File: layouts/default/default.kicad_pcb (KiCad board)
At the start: 2 copper layers, 50 x 50 mm, 37 parts

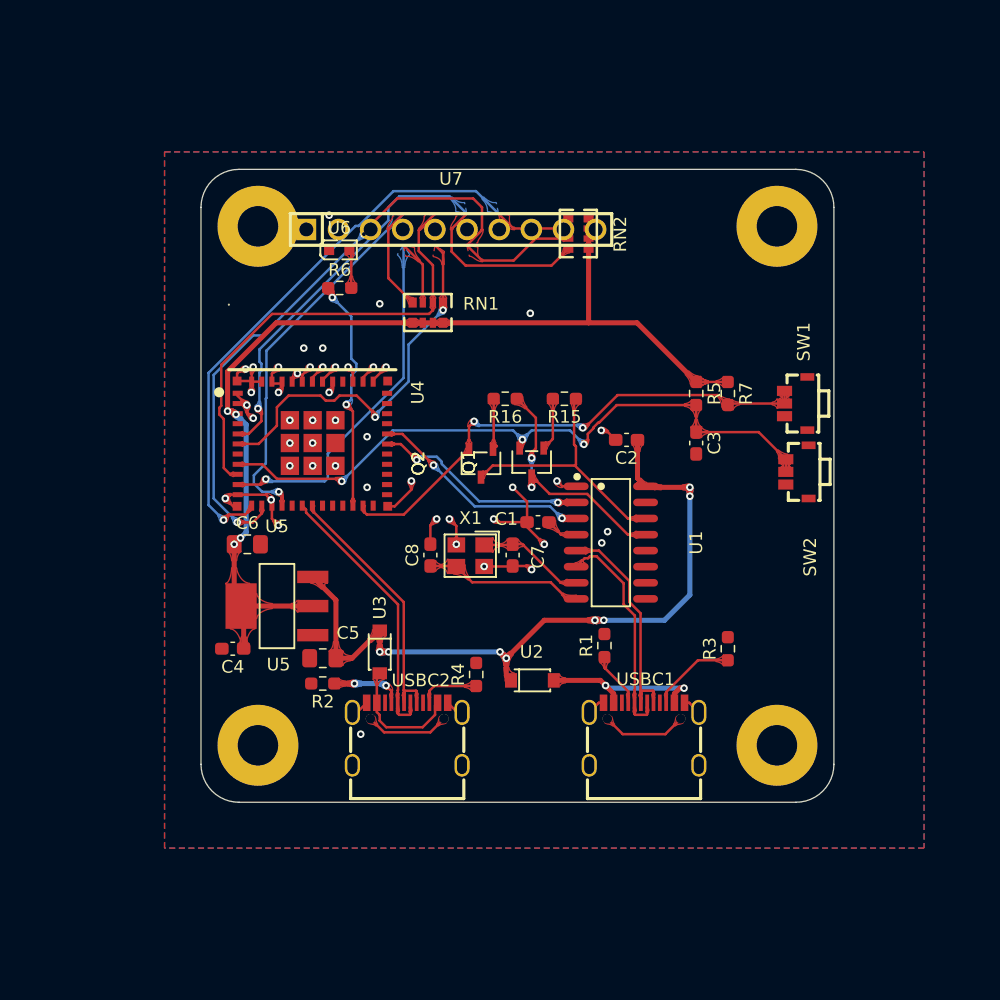
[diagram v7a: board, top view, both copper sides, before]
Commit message: New footprint for C6
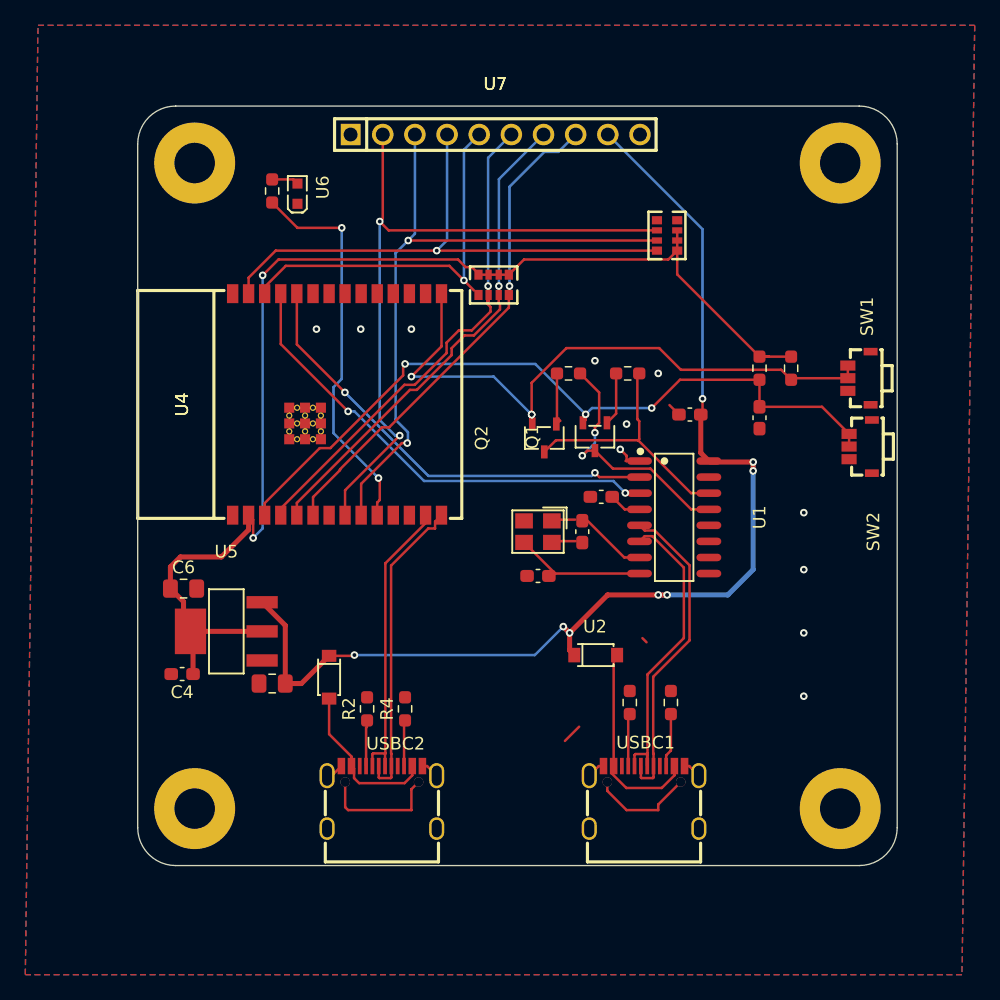
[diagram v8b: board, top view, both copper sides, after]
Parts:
- U4: footprint Espressif_Systems_ESP32_C6_MINI_1_N4:WIFIM-SMD_61P-L16.6-W13.2-P0.80-ESP32-C6-MINI-1-N4 -> Espressif_Systems_ESP32_C6_WROOM_1_N8:WIRELM-SMD_ESP32-C6-WROOM-1
- moved R6 9.34 mm to (98.5, 73.1), turned to 90 degrees
- moved C8 8.66 mm to (119.5, 103.5), turned to 180 degrees
- moved U7 8.28 mm to (116.1, 68.6)
- moved H1 7.07 mm to (92.4, 70.9)
- moved H2 7.07 mm to (143.4, 70.9)
- moved H3 7.07 mm to (92.4, 121.9)
- moved H4 7.07 mm to (143.4, 121.9)
- moved RN2 7.00 mm to (129.7, 76.6)
- moved R4 6.24 mm to (109.0, 114.0)
- moved R3 6.19 mm to (130.0, 113.5)
- moved C6 6.13 mm to (91.5, 104.5)
- moved C7 5.80 mm to (123.0, 100.0)
- moved X1 5.68 mm to (119.5, 100.0)
- moved RN1 5.65 mm to (116.0, 80.5), turned to 180 degrees
- moved U6 5.54 mm to (100.5, 73.3), turned to 90 degrees
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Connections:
- U4 pad 10: IO5 -> IO8
- U4 pad 11: GND -> IO10
- U4 pad 12: IO0 -> IO11
- U4 pad 13: IO1 -> esp32-D_N
- U4 pad 14: GND -> esp32-D_P
- U4 pad 15: IO6 -> boot_pullup-E
- U4 pad 16: IO7 -> IO18
- U4 pad 17: esp32-D_N -> IO19
- U4 pad 18: esp32-D_P -> IO20
- U4 pad 19: IO14 -> IO21
- U4 pad 2: GND -> power_3v3-VCC
- U4 pad 20: IO15 -> IO22
- U4 pad 21: esp32-net-0 -> IO23
- U4 pad 22: IO8 -> esp32-net-1
- U4 pad 23: boot_pullup-E -> IO15
- U4 pad 24: IO18 -> TXD
- U4 pad 25: IO19 -> RXD
- U4 pad 26: IO20 -> IO3
- U4 pad 27: IO21 -> IO2
- U4 pad 28: IO22 -> GND
- U4 pad 29: IO23 -> GND
- U4 pad 3: power_3v3-VCC -> btn_reset-E
- U4 pad 30: TXD -> GND
- U4 pad 31: RXD -> GND
- U4 pad 32: esp32-net-1 -> GND
- U4 pad 33: esp32-net-2 -> GND
- U4 pad 34: esp32-net-3 -> GND
- U4 pad 35: esp32-net-4 -> GND
- U4 pad 4: esp32-net-5 -> IO4
- U4 pad 5: IO2 -> IO5
- U4 pad 6: IO3 -> IO6
- U4 pad 7: esp32-net-6 -> IO7
- U4 pad 8: btn_reset-E -> IO0
- U4 pad 9: IO4 -> IO1
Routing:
- net GND: track 56.4 -> 10.8 mm, vias 47 -> 11
- net power_5v-VCC: track 60.6 -> 93.4 mm
- net RXD: track 17.7 -> 38.3 mm
- net TXD: track 17.2 -> 35.6 mm
- net power_3v3-VCC: track 81.7 -> 95.4 mm, vias 4 -> 2
- net IO8: track 18.2 -> 30.9 mm
- net boot_pullup-E: track 40.5 -> 49.7 mm, vias 2 -> 3
- net ch340g-D_P: track 18.0 -> 25.2 mm
- net ch340g-D_N: track 17.6 -> 24.4 mm
- net btn_reset-E: track 53.1 -> 59.7 mm
- net IO5: track 33.5 -> 39.0 mm
- net IO0: track 50.3 -> 55.0 mm, vias 1 -> 2
- net diode_esp-VBUS: track 9.36 -> 12.8 mm
- net esp32-D_P: track 21.4 -> 24.6 mm
- net footprint-net-1: track 6.69 -> 9.77 mm
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- removed copper zone on F.Cu, net A
- removed copper zone on B.Cu, net IO0
- removed copper zone on F.Cu, net IO0
- removed copper zone on B.Cu, net IO1
- removed copper zone on F.Cu, net IO1
- removed copper zone on B.Cu, net IO2
- removed copper zone on F.Cu, net IO2
- removed copper zone on B.Cu, net IO3
- removed copper zone on F.Cu, net IO3
- removed copper zone on F.Cu, net IO4
- removed copper zone on B.Cu, net IO5
- removed copper zone on F.Cu, net IO5
- removed copper zone on B.Cu, net IO6
- removed copper zone on F.Cu, net IO6
- removed copper zone on B.Cu, net IO8
- removed copper zone on F.Cu, net IO8
- removed copper zone on B.Cu, net RXD
- removed copper zone on F.Cu, net RXD
- removed copper zone on B.Cu, net TXD
- removed copper zone on F.Cu, net TXD
- removed copper zone on F.Cu, net V3
- removed copper zone on F.Cu, net XI
- removed copper zone on F.Cu, net XO
- removed copper zone on B.Cu, net boot_pullup-E
- removed copper zone on F.Cu, net boot_pullup-E
- removed copper zone on B.Cu, net btn_reset-E
- removed copper zone on F.Cu, net btn_reset-E
- removed copper zone on F.Cu, net cc1_r_debug-A5
- removed copper zone on B.Cu, net cc1_r_esp-A5
- removed copper zone on F.Cu, net cc1_r_esp-A5
- removed copper zone on F.Cu, net cc2_r_debug-B5
- removed copper zone on F.Cu, net cc2_r_esp-B5
- removed copper zone on B.Cu, net ch340g-C-0
- removed copper zone on F.Cu, net ch340g-C-0
- removed copper zone on F.Cu, net ch340g-C-1
- removed copper zone on F.Cu, net ch340g-D_N
- removed copper zone on F.Cu, net ch340g-D_P
- removed copper zone on F.Cu, net diode_debug-VBUS
- removed copper zone on F.Cu, net diode_esp-VBUS
- removed copper zone on F.Cu, net esp32-D_N
- removed copper zone on F.Cu, net esp32-D_P
- removed copper zone on F.Cu, net footprint-B-0
- removed copper zone on F.Cu, net footprint-B-1
- removed copper zone on F.Cu, net footprint-net-0
- removed copper zone on F.Cu, net footprint-net-1
- removed copper zone on B.Cu, net power_3v3-VCC
- removed copper zone on F.Cu, net power_3v3-VCC
- removed copper zone on B.Cu, net power_5v-VCC
- removed copper zone on F.Cu, net power_5v-VCC
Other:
- board size 50 x 50 mm -> 60 x 60 mm
